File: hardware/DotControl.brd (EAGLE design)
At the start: 30.7 x 65 mm, 34 parts, among them CN1 1X4-BIG, J3 USB-MICROB, SW2 Previous, SW5 Previous, SW6 Next, SW8 Ok, U1 ATMEGA328P-MU-QFN32, U2 TMP102, U3 ATSHA204-TSU

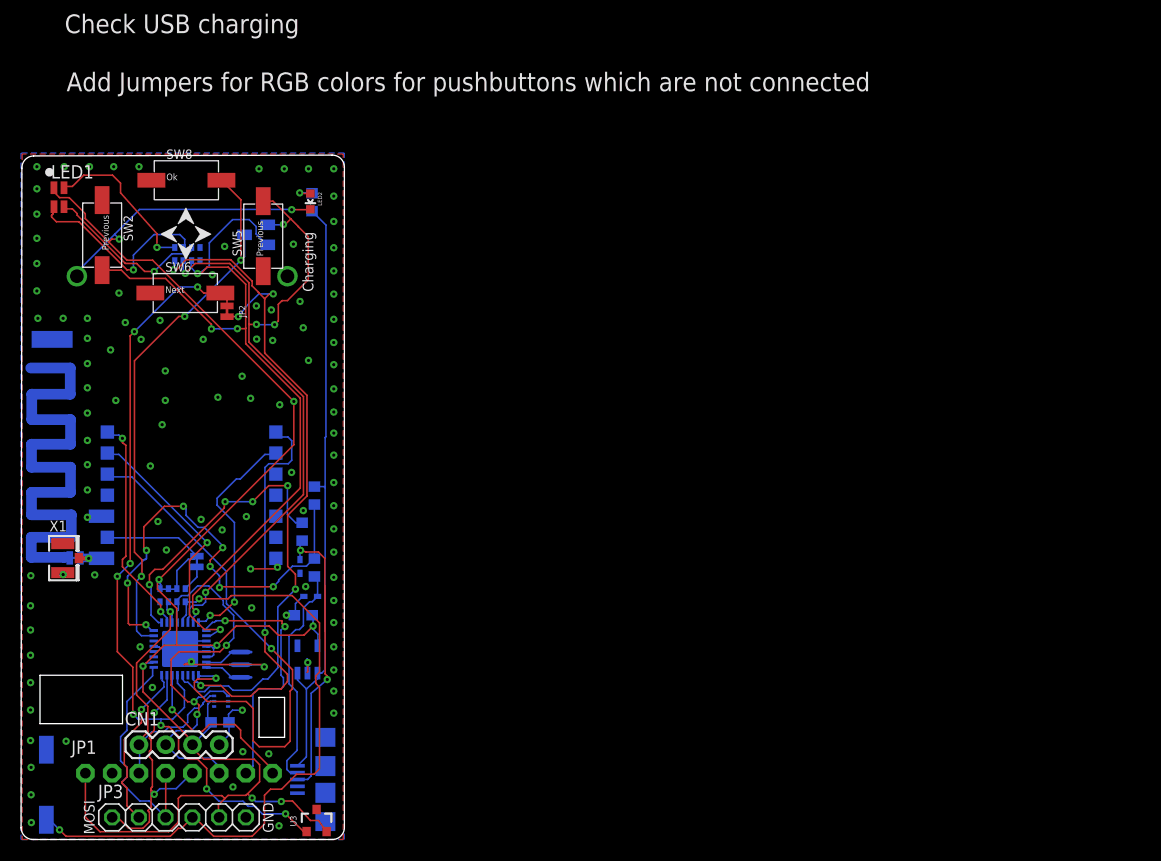
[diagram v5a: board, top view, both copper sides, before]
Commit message: Add Si7021 temp sensor
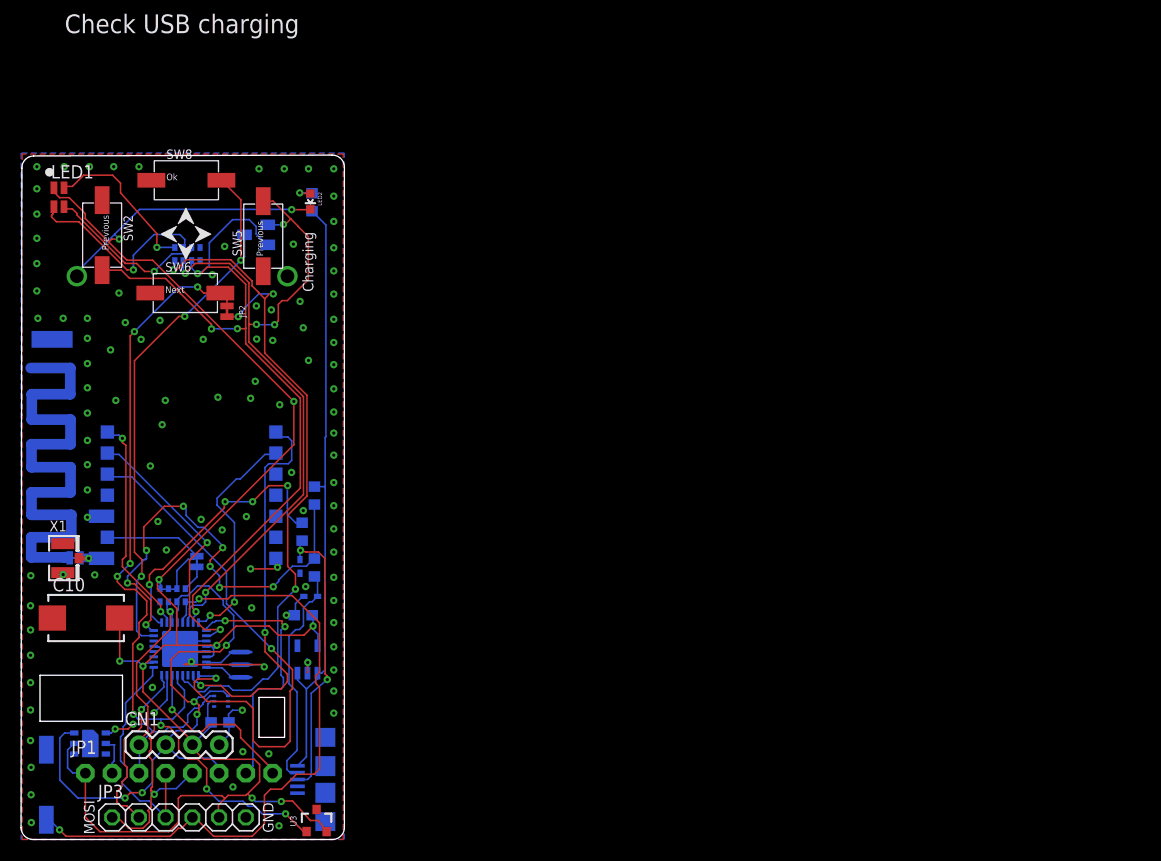
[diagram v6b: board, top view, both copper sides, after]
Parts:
- added C10: 1500uF 4V, adafruit:CT7343
- added U4: SI7021, SparkFun-Sensors:DFN-6-3X3-SI7021
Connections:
- net +3V3: now also C10.+, U4.VDD
- net GND: now also C10.-, U4.GND
- net SCL: now also U4.SCK
- net SDA: now also U4.DATA
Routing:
- net SCL: track 34.2 -> 54.0 mm, vias 3 -> 5
- net +3V3: track 189.8 -> 200.8 mm, vias 9 -> 10
- net SDA: track 26.7 -> 31.8 mm, vias 1 -> 3
- net GND: track 38.9 -> 42.6 mm, vias 108 -> 106
- net ADCENA: track 78.9 -> 80.6 mm
- net MISO: track 16.1 -> 17.1 mm
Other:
- outline, holes or cut-outs redrawn
- board text removed: "Add Jumpers for RGB colors for pushbuttons which are not connected"

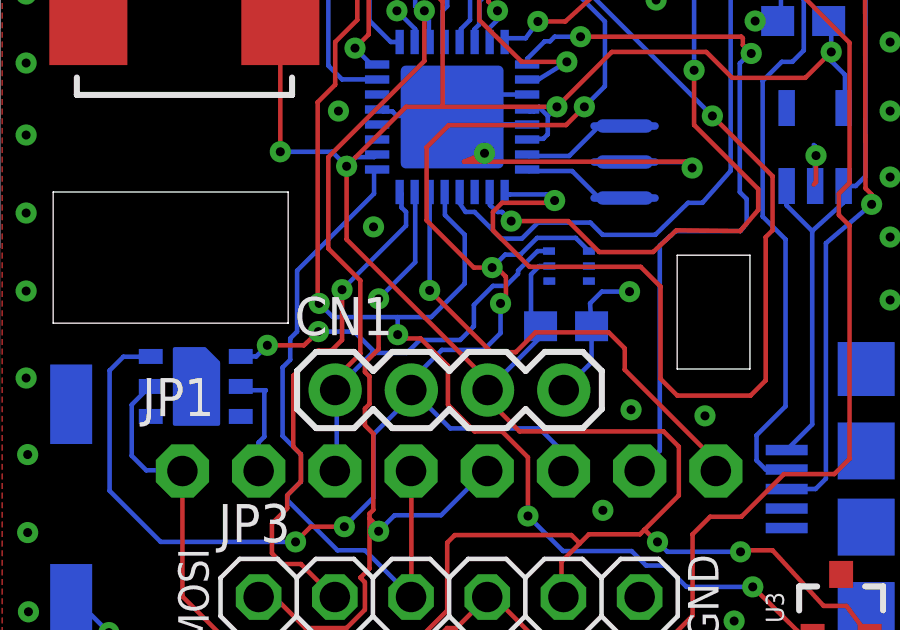
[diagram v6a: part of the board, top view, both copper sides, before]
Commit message: Add I2C text
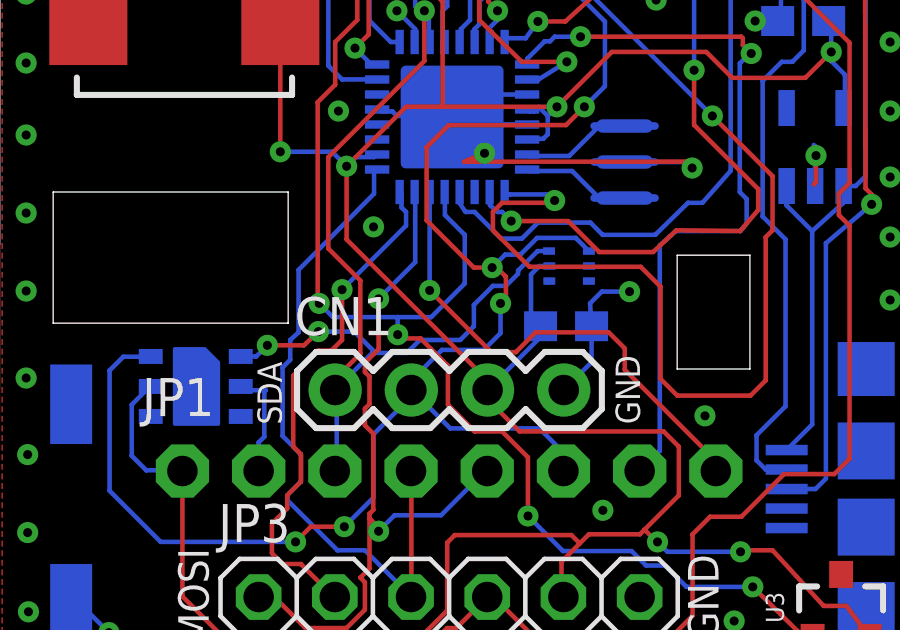
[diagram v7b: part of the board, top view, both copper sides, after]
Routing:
- net GND: vias 106 -> 105
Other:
- board text added: "SDA"
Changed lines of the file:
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@@
 <rectangle x1="0.1524" y1="25.527" x2="5.6134" y2="48.9712" layer="42"/>
 <text x="4.1402" y="76.581" size="1.778" layer="21">Check USB charging</text>
+<text x="9.4234" y="7.8486" size="0.8128" layer="21" rot="R90">SDA</text>
+<text x="20.5486" y="10.16" size="0.8128" layer="21" rot="R270">GND</text>
 </plain>
 <attributes>
@@
 <via x="21.0132" y="12.2794" extent="1-16" drill="0.3"/>
 <via x="20.1242" y="4.9896" extent="1-16" drill="0.3"/>
-<via x="21.064" y="8.3424" extent="1-16" drill="0.3"/>
 <wire x1="16.1798" y1="17.018" x2="16.1798" y2="17.8308" width="0.1524" layer="16"/>
 <wire x1="16.1798" y1="17.8308" x2="17.4752" y2="17.8308" width="0.1524" layer="16"/>
@@
 <contactref element="U1" pad="17"/>
 <wire x1="12.4968" y1="15.5448" x2="12.4968" y2="16.3068" width="0.1524" layer="16"/>
-<wire x1="9.9314" y1="12.9794" x2="12.4968" y2="15.5448" width="0.1524" layer="16"/>
+<wire x1="9.9822" y1="13.0048" x2="12.4968" y2="15.5448" width="0.1524" layer="16"/>
 <wire x1="9.4488" y1="7.4676" x2="9.4488" y2="9.7536" width="0.1524" layer="16"/>
 <wire x1="10.0584" y1="5.9436" x2="10.0584" y2="6.858" width="0.1524" layer="16"/>
@@
 <wire x1="13.716" y1="2.1336" x2="13.73" y2="2.1" width="0.1524" layer="16"/>
 <wire x1="9.4488" y1="7.4676" x2="10.0584" y2="6.858" width="0.1524" layer="16"/>
-<wire x1="9.9314" y1="12.9794" x2="9.9314" y2="10.9474" width="0.1524" layer="16"/>
-<wire x1="9.9314" y1="10.9474" x2="9.7028" y2="10.7188" width="0.1524" layer="16"/>
-<wire x1="9.7028" y1="10.7188" x2="9.7028" y2="10.0076" width="0.1524" layer="16"/>
+<wire x1="9.9822" y1="13.0048" x2="9.9822" y2="10.922" width="0.1524" layer="16"/>
+<wire x1="9.9822" y1="10.922" x2="9.7028" y2="10.668" width="0.1524" layer="16"/>
+<wire x1="9.7028" y1="10.668" x2="9.7028" y2="10.0076" width="0.1524" layer="16"/>
 <wire x1="9.7028" y1="10.0076" x2="9.4488" y2="9.7536" width="0.1524" layer="16"/>
 </signal>

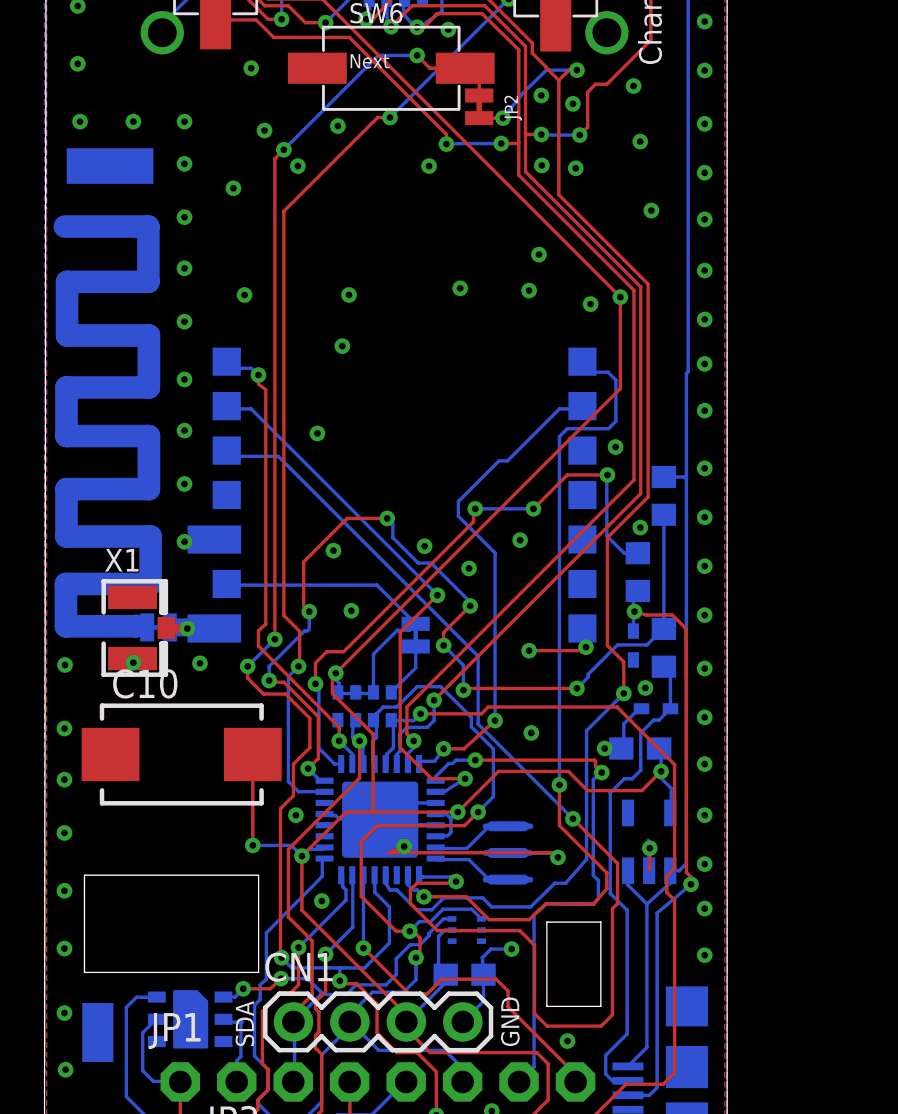
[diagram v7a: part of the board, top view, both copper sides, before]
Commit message: [Beta] Add HW support for MPU9250
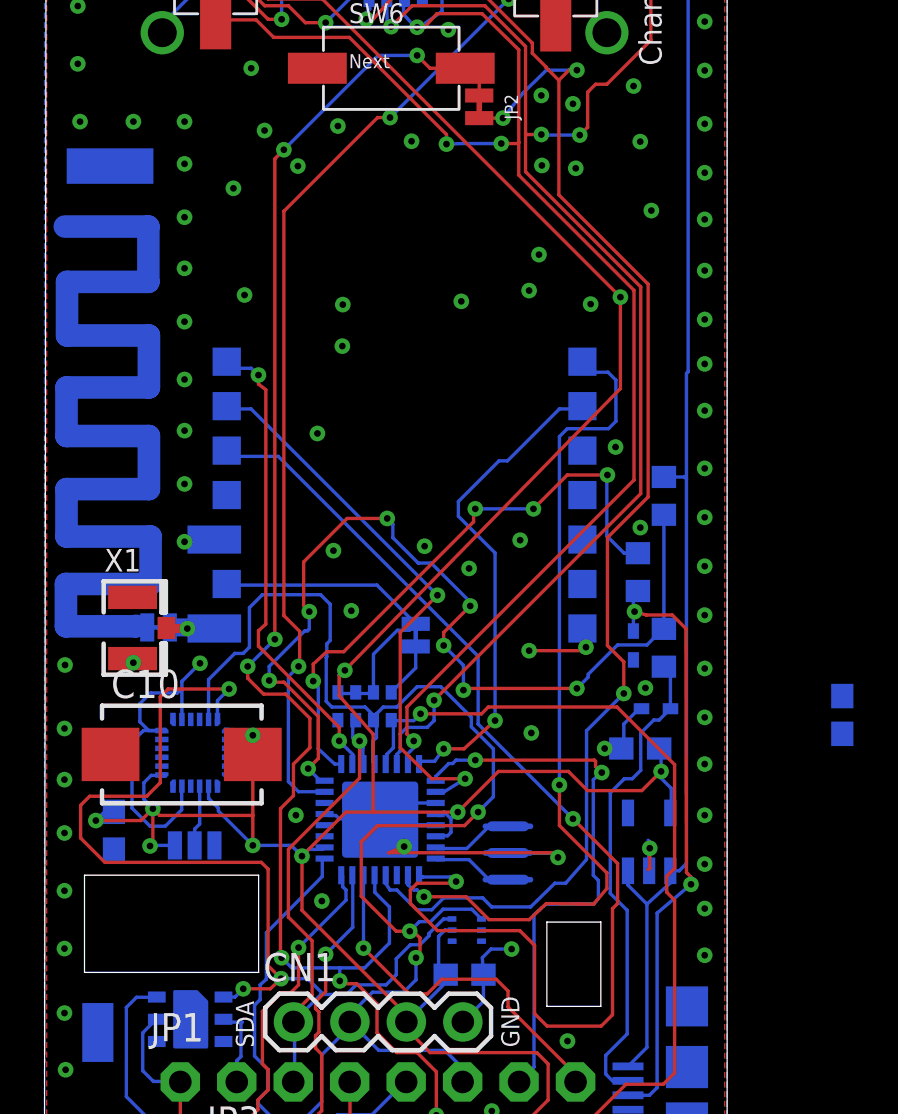
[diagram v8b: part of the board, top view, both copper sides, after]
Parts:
- added C4, C8: 0.1uF, resistor:C0603
- added SJ5: (no value), SparkFun:SJ_3
- added U5: 9DoF IMU, SparkFun-Sensors:QFN24-3X3
- moved U$2 0.07 mm to (15.7, 61.0), turned to 90 degrees
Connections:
- new net MOVE_INT: U5.12
- new net N$10: SJ5.2, U5.9
- new net N$15: C8.1, U5.10
- net +3V3: now also C4.1, SJ5.3, U5.1, U5.13, U5.8
- net GND: now also C4.2, C8.2, SJ5.1, U5.11, U5.18, U5.20
- net SCL: now also U5.23
- net SDA: now also U5.24
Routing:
- net SDA: track 31.8 -> 60.1 mm, vias 3 -> 4
- net +3V3: track 200.8 -> 219.5 mm, vias 10 -> 14
- net SCL: track 54.0 -> 71.1 mm
- net GND: track 42.6 -> 58.0 mm
- net N$10: track 0.00 -> 2.76 mm
